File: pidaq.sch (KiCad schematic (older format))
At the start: 41 parts, among them J1 Screw_Terminal_01x08, J2 Screw_Terminal_01x08, J3 Screw_Terminal_01x10, J4 Screw_Terminal_01x10, J5 Conn_01x02_Male, J6 Conn_01x08_Female, U1 LTC2984CLX-DNP, U2 LTC2418IGN-DNP

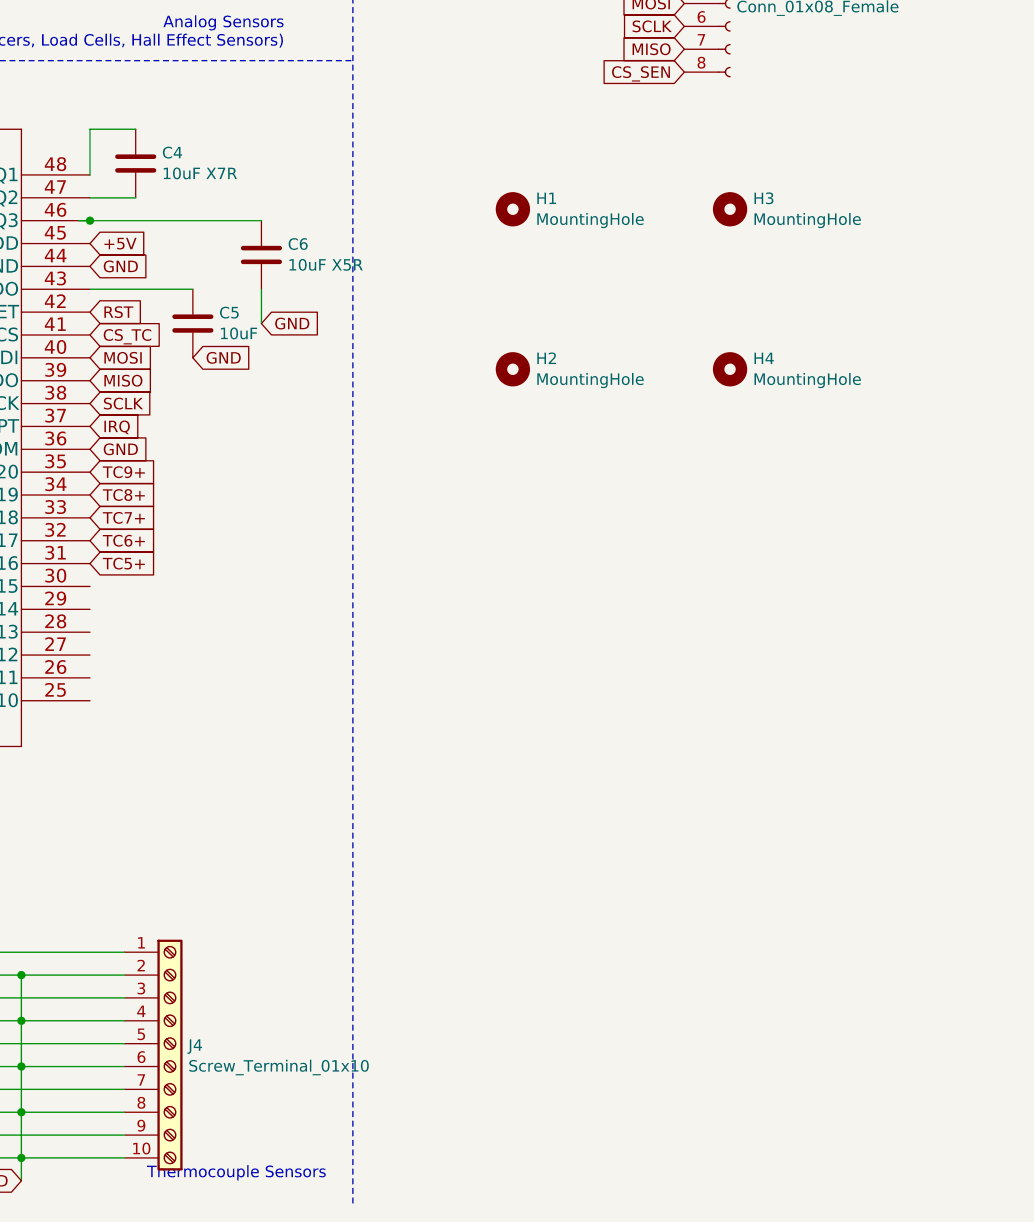
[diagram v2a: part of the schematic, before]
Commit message: added more bom details
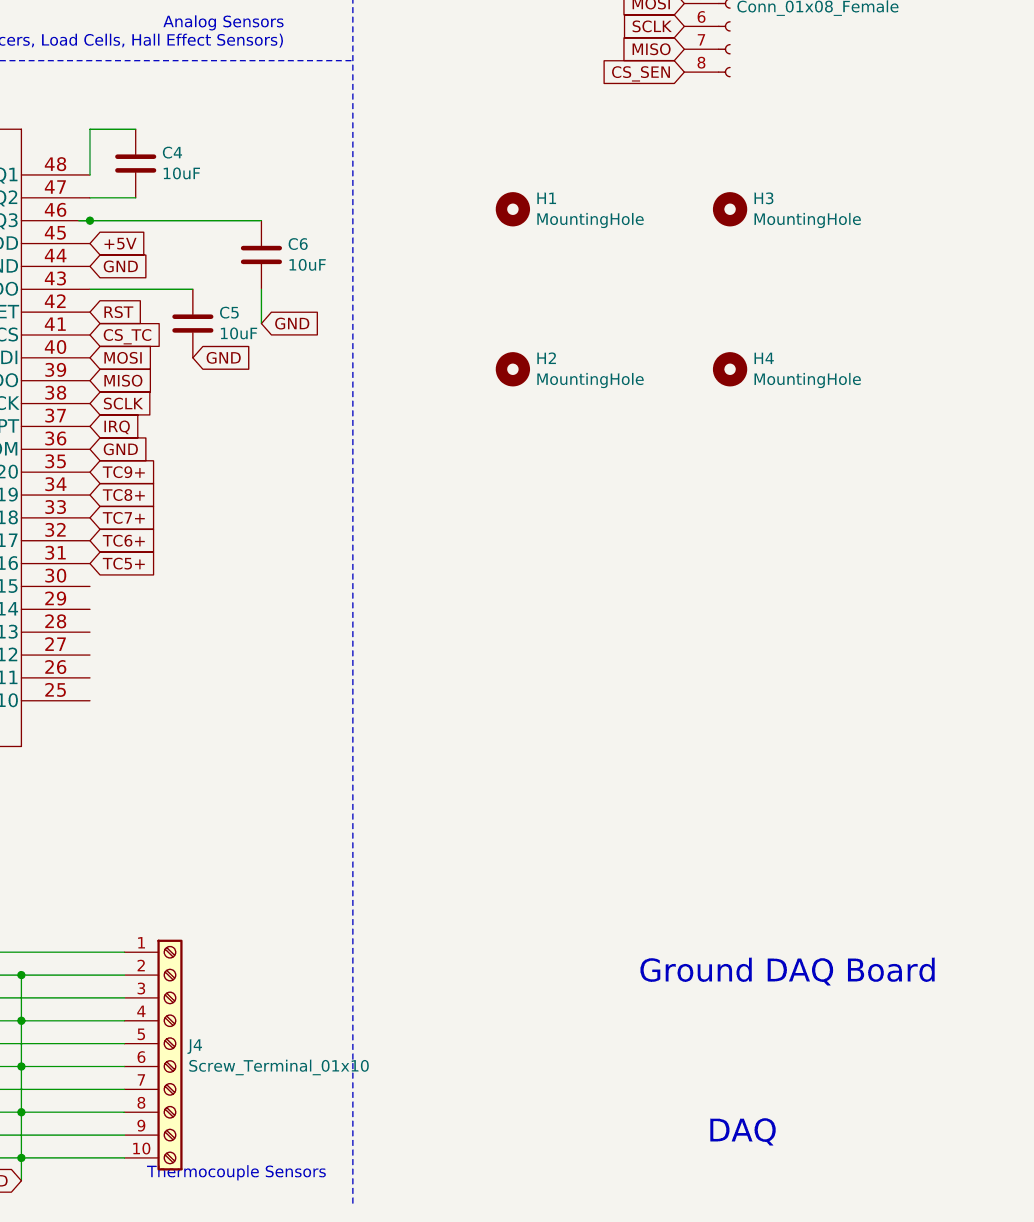
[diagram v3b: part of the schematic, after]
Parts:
- C1: Dielectric (none) -> tantalum
- C10, C11, C12, C13, C14, C18, C19, C2, C20, C21, C22, C3, C5, C7, C8: Dielectric (none) -> ceramic
- C4: value 10uF X7R -> 10uF; Dielectric (none) -> X7R
- C6: value 10uF X5R -> 10uF; Dielectric (none) -> X5R
- D1, U1, U2: place? (none) -> DNP
- R12, R13, R14, R15, R16, R4, R5, R6, R7, R8: Tolerance (none) -> 1%
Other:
- note added: "DAQ"
- note added: "Ground DAQ Board"
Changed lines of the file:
@@
 F 2 "proj_footprints:LTC2418IGN-PBF" H 2850 1190 60  0001 C CNN
 F 3 "" H 1750 950 60  0000 C CNN
+F 4 "DNP" H 1750 950 50  0001 C CNN "place?"
 	1    1750 950
 	1    0    0    -1
@@
 F 2 "Capacitor_SMD:C_0805_2012Metric_Pad1.15x1.40mm_HandSolder" H 788 2050 50  0001 C CNN
 F 3 "~" H 750 2200 50  0001 C CNN
+F 4 "tantalum" H 750 2200 50  0001 C CNN "Dielectric"
 	1    750  2200
 	1    0    0    -1
@@
 F 2 "Capacitor_SMD:C_0805_2012Metric_Pad1.15x1.40mm_HandSolder" H 1188 2050 50  0001 C CNN
 F 3 "~" H 1150 2200 50  0001 C CNN
+F 4 "ceramic" H 1150 2200 50  0001 C CNN "Dielectric"
 	1    1150 2200
 	1    0    0    -1
@@
 P 4950 3250
 F 0 "C4" H 5065 3296 50  0000 L CNN
-F 1 "10uF X7R" H 5065 3205 50  0000 L CNN
+F 1 "10uF" H 5065 3205 50  0000 L CNN
 F 2 "Capacitor_SMD:C_0805_2012Metric_Pad1.15x1.40mm_HandSolder" H 4988 3100 50  0001 C CNN
 F 3 "~" H 4950 3250 50  0001 C CNN
+F 4 "X7R" H 4950 3250 50  0001 C CNN "Dielectric"
 	1    4950 3250
 	1    0    0    -1
@@
 P 5500 3650
 F 0 "C6" H 5615 3696 50  0000 L CNN
-F 1 "10uF X5R" H 5615 3605 50  0000 L CNN
+F 1 "10uF" H 5615 3605 50  0000 L CNN
 F 2 "Capacitor_SMD:C_0805_2012Metric_Pad1.15x1.40mm_HandSolder" H 5538 3500 50  0001 C CNN
 F 3 "~" H 5500 3650 50  0001 C CNN
+F 4 "X5R" H 5500 3650 50  0001 C CNN "Dielectric"
 	1    5500 3650
 	1    0    0    -1
@@
 F 2 "Capacitor_SMD:C_0805_2012Metric_Pad1.15x1.40mm_HandSolder" H 5238 3800 50  0001 C CNN
 F 3 "~" H 5200 3950 50  0001 C CNN
+F 4 "ceramic" H 5200 3950 50  0001 C CNN "Dielectric"
 	1    5200 3950
 	1    0    0    -1
@@
 F 2 "Capacitor_SMD:C_0805_2012Metric_Pad1.15x1.40mm_HandSolder" H 738 4600 50  0001 C CNN
 F 3 "~" H 700 4750 50  0001 C CNN
+F 4 "ceramic" H 700 4750 50  0001 C CNN "Dielectric"
 	1    700  4750
 	1    0    0    -1
@@
 F 2 "proj_footprints:LTC2984CLX-PBF" H 3150 3540 60  0001 C CNN
 F 3 "" H 1550 3300 60  0000 C CNN
+F 4 "DNP" H 1550 3300 50  0001 C CNN "place?"
 	1    1550 3300
 	1    0    0    -1
@@
 F 2 "Capacitor_SMD:C_0805_2012Metric_Pad1.15x1.40mm_HandSolder" H 4250 7600 50  0001 C CNN
 F 3 "~" H 4250 7600 50  0001 C CNN
+F 4 "ceramic" H 4250 7600 50  0001 C CNN "Dielectric"
 	1    4250 7600
 	0    1    1    0
@@
 F 2 "Resistor_SMD:R_0805_2012Metric_Pad1.15x1.40mm_HandSolder" H 4050 7500 50  0001 C CNN
 F 3 "~" H 4050 7500 50  0001 C CNN
+F 4 "1%" H 4050 7500 50  0001 C CNN "Tolerance"
 	1    4050 7500
 	0    1    1    0
@@
 F 2 "Capacitor_SMD:C_0805_2012Metric_Pad1.15x1.40mm_HandSolder" H 4250 7400 50  0001 C CNN
 F 3 "~" H 4250 7400 50  0001 C CNN
+F 4 "ceramic" H 4250 7400 50  0001 C CNN "Dielectric"
 	1    4250 7400
 	0    1    1    0
@@
 F 2 "Resistor_SMD:R_0805_2012Metric_Pad1.15x1.40mm_HandSolder" H 4050 7300 50  0001 C CNN
 F 3 "~" H 4050 7300 50  0001 C CNN
+F 4 "1%" H 4050 7300 50  0001 C CNN "Tolerance"
 	1    4050 7300
 	0    1    1    0
@@
 F 2 "Capacitor_SMD:C_0805_2012Metric_Pad1.15x1.40mm_HandSolder" H 4250 7200 50  0001 C CNN
 F 3 "~" H 4250 7200 50  0001 C CNN
+F 4 "ceramic" H 4250 7200 50  0001 C CNN "Dielectric"
 	1    4250 7200
 	0    1    1    0
@@
 F 2 "Resistor_SMD:R_0805_2012Metric_Pad1.15x1.40mm_HandSolder" H 4050 7100 50  0001 C CNN
 F 3 "~" H 4050 7100 50  0001 C CNN
+F 4 "1%" H 4050 7100 50  0001 C CNN "Tolerance"
 	1    4050 7100
 	0    1    1    0
@@
 F 2 "Capacitor_SMD:C_0805_2012Metric_Pad1.15x1.40mm_HandSolder" H 4250 7000 50  0001 C CNN
 F 3 "~" H 4250 7000 50  0001 C CNN
+F 4 "ceramic" H 4250 7000 50  0001 C CNN "Dielectric"
 	1    4250 7000
 	0    1    1    0
@@
 F 2 "Resistor_SMD:R_0805_2012Metric_Pad1.15x1.40mm_HandSolder" H 4050 6900 50  0001 C CNN
 F 3 "~" H 4050 6900 50  0001 C CNN
+F 4 "1%" H 4050 6900 50  0001 C CNN "Tolerance"
 	1    4050 6900
 	0    1    1    0
@@
 F 2 "Capacitor_SMD:C_0805_2012Metric_Pad1.15x1.40mm_HandSolder" H 4250 6800 50  0001 C CNN
 F 3 "~" H 4250 6800 50  0001 C CNN
+F 4 "ceramic" H 4250 6800 50  0001 C CNN "Dielectric"
 	1    4250 6800
 	0    1    1    0
@@
 F 2 "Resistor_SMD:R_0805_2012Metric_Pad1.15x1.40mm_HandSolder" H 4050 6700 50  0001 C CNN
 F 3 "~" H 4050 6700 50  0001 C CNN
+F 4 "1%" H 4050 6700 50  0001 C CNN "Tolerance"
 	1    4050 6700
 	0    1    1    0
@@
 F 2 "Capacitor_SMD:C_0805_2012Metric_Pad1.15x1.40mm_HandSolder" H 1550 7600 50  0001 C CNN
 F 3 "~" H 1550 7600 50  0001 C CNN
+F 4 "ceramic" H 1550 7600 50  0001 C CNN "Dielectric"
 	1    1550 7600
 	0    1    1    0
@@
 F 2 "Resistor_SMD:R_0805_2012Metric_Pad1.15x1.40mm_HandSolder" H 1350 7500 50  0001 C CNN
 F 3 "~" H 1350 7500 50  0001 C CNN
+F 4 "1%" H 1350 7500 50  0001 C CNN "Tolerance"
 	1    1350 7500
 	0    1    1    0
@@
 F 2 "Capacitor_SMD:C_0805_2012Metric_Pad1.15x1.40mm_HandSolder" H 1550 7400 50  0001 C CNN
 F 3 "~" H 1550 7400 50  0001 C CNN
+F 4 "ceramic" H 1550 7400 50  0001 C CNN "Dielectric"
 	1    1550 7400
 	0    1    1    0
@@
 F 2 "Resistor_SMD:R_0805_2012Metric_Pad1.15x1.40mm_HandSolder" H 1350 7300 50  0001 C CNN
 F 3 "~" H 1350 7300 50  0001 C CNN
+F 4 "1%" H 1350 7300 50  0001 C CNN "Tolerance"
 	1    1350 7300
 	0    1    1    0
@@
 F 2 "Capacitor_SMD:C_0805_2012Metric_Pad1.15x1.40mm_HandSolder" H 1550 7200 50  0001 C CNN
 F 3 "~" H 1550 7200 50  0001 C CNN
+F 4 "ceramic" H 1550 7200 50  0001 C CNN "Dielectric"
 	1    1550 7200
 	0    1    1    0
@@
 F 2 "Resistor_SMD:R_0805_2012Metric_Pad1.15x1.40mm_HandSolder" H 1350 7100 50  0001 C CNN
 F 3 "~" H 1350 7100 50  0001 C CNN
+F 4 "1%" H 1350 7100 50  0001 C CNN "Tolerance"
 	1    1350 7100
 	0    1    1    0
@@
 F 2 "Capacitor_SMD:C_0805_2012Metric_Pad1.15x1.40mm_HandSolder" H 1550 7000 50  0001 C CNN
 F 3 "~" H 1550 7000 50  0001 C CNN
+F 4 "ceramic" H 1550 7000 50  0001 C CNN "Dielectric"
 	1    1550 7000
 	0    1    1    0
@@
 F 2 "Resistor_SMD:R_0805_2012Metric_Pad1.15x1.40mm_HandSolder" H 1350 6900 50  0001 C CNN
 F 3 "~" H 1350 6900 50  0001 C CNN
+F 4 "1%" H 1350 6900 50  0001 C CNN "Tolerance"
 	1    1350 6900
 	0    1    1    0
@@
 F 2 "Capacitor_SMD:C_0805_2012Metric_Pad1.15x1.40mm_HandSolder" H 1550 6800 50  0001 C CNN
 F 3 "~" H 1550 6800 50  0001 C CNN
+F 4 "ceramic" H 1550 6800 50  0001 C CNN "Dielectric"
 	1    1550 6800
 	0    1    1    0
@@
 F 2 "Resistor_SMD:R_0805_2012Metric_Pad1.15x1.40mm_HandSolder" H 1350 6700 50  0001 C CNN
 F 3 "~" H 1350 6700 50  0001 C CNN
+F 4 "1%" H 1350 6700 50  0001 C CNN "Tolerance"
 	1    1350 6700
 	0    1    1    0
@@
 F 2 "Diode_THT:D_DO-35_SOD27_P7.62mm_Horizontal" H 900 4875 50  0001 C CNN
 F 3 "https://assets.nexperia.com/documents/data-sheet/1N4148_1N4448.pdf" H 900 5050 50  0001 C CNN
+F 4 "DNP" H 900 5050 50  0001 C CNN "place?"
 	1    900  5050
 	0    -1   -1   0
@@
 F 2 "Capacitor_SMD:C_0805_2012Metric_Pad1.15x1.40mm_HandSolder" H 688 3900 50  0001 C CNN
 F 3 "~" H 650 4050 50  0001 C CNN
+F 4 "ceramic" H 650 4050 50  0001 C CNN "Dielectric"
 	1    650  4050
 	1    0    0    -1
@@
 F 2 "Capacitor_SMD:C_0805_2012Metric_Pad1.15x1.40mm_HandSolder" H 1038 3600 50  0001 C CNN
 F 3 "~" H 1000 3750 50  0001 C CNN
+F 4 "ceramic" H 1000 3750 50  0001 C CNN "Dielectric"
 	1    1000 3750
 	1    0    0    -1
@@
 Text GLabel 1000 3900 0    50   Input ~ 0
 GND
+Text Notes 7150 6850 0    100  ~ 0
+Ground DAQ Board
+Text Notes 7450 7550 0    100  ~ 0
+DAQ
 $EndSCHEMATC

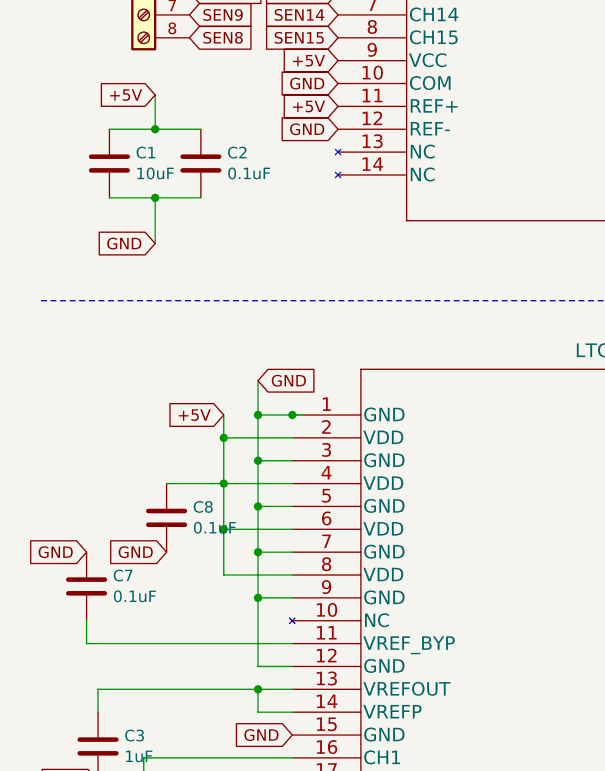
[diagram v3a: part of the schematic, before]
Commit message: convert uF to nF for better BOM compatibility
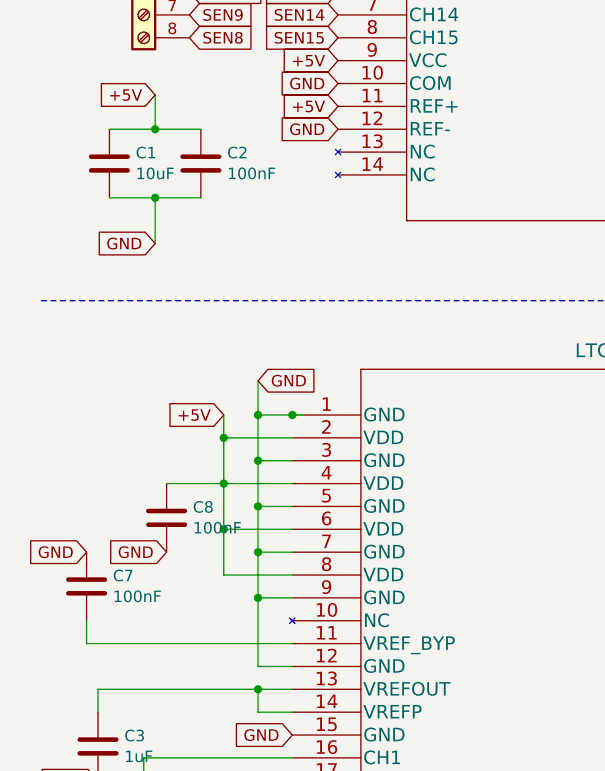
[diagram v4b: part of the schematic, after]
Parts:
- C2, C7, C8: value 0.1uF -> 100nF
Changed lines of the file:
@@
 AR Path="/5ED56214/5EDBB98B" Ref="C?"  Part="1"
 F 0 "C2" H 1265 2246 50  0000 L CNN
-F 1 "0.1uF" H 1265 2155 50  0000 L CNN
+F 1 "100nF" H 1265 2155 50  0000 L CNN
 F 2 "Capacitor_SMD:C_0805_2012Metric_Pad1.15x1.40mm_HandSolder" H 1188 2050 50  0001 C CNN
 F 3 "~" H 1150 2200 50  0001 C CNN
@@
 P 650 4050
 F 0 "C7" H 765 4096 50  0000 L CNN
-F 1 "0.1uF" H 765 4005 50  0000 L CNN
+F 1 "100nF" H 765 4005 50  0000 L CNN
 F 2 "Capacitor_SMD:C_0805_2012Metric_Pad1.15x1.40mm_HandSolder" H 688 3900 50  0001 C CNN
 F 3 "~" H 650 4050 50  0001 C CNN
@@
 P 1000 3750
 F 0 "C8" H 1115 3796 50  0000 L CNN
-F 1 "0.1uF" H 1115 3705 50  0000 L CNN
+F 1 "100nF" H 1115 3705 50  0000 L CNN
 F 2 "Capacitor_SMD:C_0805_2012Metric_Pad1.15x1.40mm_HandSolder" H 1038 3600 50  0001 C CNN
 F 3 "~" H 1000 3750 50  0001 C CNN
